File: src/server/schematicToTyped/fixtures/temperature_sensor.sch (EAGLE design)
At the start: 1 part, among them U1 MCP9808

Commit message: Improve fixtures
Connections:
- net <SCL renamed #I2C4.SCL_3.3V
- net <SDA renamed #I2C4.SDA_3.3V
- new net #GPIO0_3.3V: U1.ALERT
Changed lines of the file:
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@@
 <?xml version="1.0" encoding="utf-8"?>
 <!DOCTYPE eagle SYSTEM "eagle.dtd">
-<eagle version="9.2.2">
+<eagle version="9.6.2">
 <drawing>
 <settings>
@@
 </segment>
 </net>
-<net name="&lt;SCL" class="0">
+<net name="#I2C4.SCL_3.3V" class="0">
 <segment>
 <pinref part="U1" gate="G$1" pin="SCL"/>
-<wire x1="-2.54" y1="-10.16" x2="-2.54" y2="-15.24" width="0.1524" layer="91"/>
-<wire x1="-2.54" y1="-15.24" x2="5.08" y2="-15.24" width="0.1524" layer="91"/>
+<wire x1="-2.54" y1="-10.16" x2="-2.54" y2="-17.78" width="0.1524" layer="91"/>
+<wire x1="-2.54" y1="-17.78" x2="5.08" y2="-17.78" width="0.1524" layer="91"/>
+<label x="5.08" y="-17.78" size="1.27" layer="95" xref="yes"/>
+</segment>
+</net>
+<net name="#I2C4.SDA_3.3V" class="0">
+<segment>
+<pinref part="U1" gate="G$1" pin="SDA"/>
+<wire x1="0" y1="-10.16" x2="0" y2="-15.24" width="0.1524" layer="91"/>
+<wire x1="0" y1="-15.24" x2="5.08" y2="-15.24" width="0.1524" layer="91"/>
 <label x="5.08" y="-15.24" size="1.27" layer="95" xref="yes"/>
 </segment>
 </net>
-<net name="&lt;SDA" class="0">
-<segment>
-<pinref part="U1" gate="G$1" pin="SDA"/>
-<wire x1="0" y1="-10.16" x2="0" y2="-12.7" width="0.1524" layer="91"/>
-<wire x1="0" y1="-12.7" x2="5.08" y2="-12.7" width="0.1524" layer="91"/>
+<net name="#GPIO0_3.3V" class="0">
+<segment>
+<pinref part="U1" gate="G$1" pin="ALERT"/>
+<wire x1="2.54" y1="-10.16" x2="2.54" y2="-12.7" width="0.1524" layer="91"/>
+<wire x1="2.54" y1="-12.7" x2="5.08" y2="-12.7" width="0.1524" layer="91"/>
 <label x="5.08" y="-12.7" size="1.27" layer="95" xref="yes"/>
 </segment>

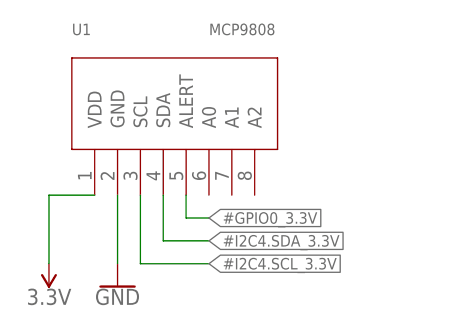
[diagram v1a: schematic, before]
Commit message: Adding support for range and list of voltages
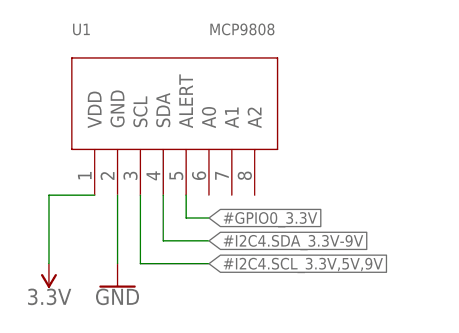
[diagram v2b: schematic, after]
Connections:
- net #I2C4.SCL_3.3V renamed #I2C4.SCL_3.3V,5V,9V
- net #I2C4.SDA_3.3V renamed #I2C4.SDA_3.3V-9V
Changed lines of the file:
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@@
 </segment>
 </net>
-<net name="#I2C4.SCL_3.3V" class="0">
+<net name="#I2C4.SCL_3.3V,5V,9V" class="0">
 <segment>
 <pinref part="U1" gate="G$1" pin="SCL"/>
@@
 </segment>
 </net>
-<net name="#I2C4.SDA_3.3V" class="0">
+<net name="#I2C4.SDA_3.3V-9V" class="0">
 <segment>
 <pinref part="U1" gate="G$1" pin="SDA"/>

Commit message: Improving typed schematics
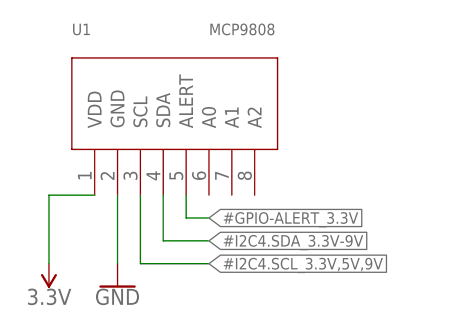
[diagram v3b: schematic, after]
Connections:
- net #GPIO0_3.3V renamed #GPIO-ALERT_3.3V
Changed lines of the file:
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@@
 </segment>
 </net>
-<net name="#GPIO0_3.3V" class="0">
+<net name="#GPIO-ALERT_3.3V" class="0">
 <segment>
 <pinref part="U1" gate="G$1" pin="ALERT"/>
